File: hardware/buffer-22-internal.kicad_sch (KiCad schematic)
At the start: 9 parts, among them U6 SN74LVC8T245DWRG4, U7 SN74LVC8T245DWRG4, U8 SN74LVC8T245DWRG4

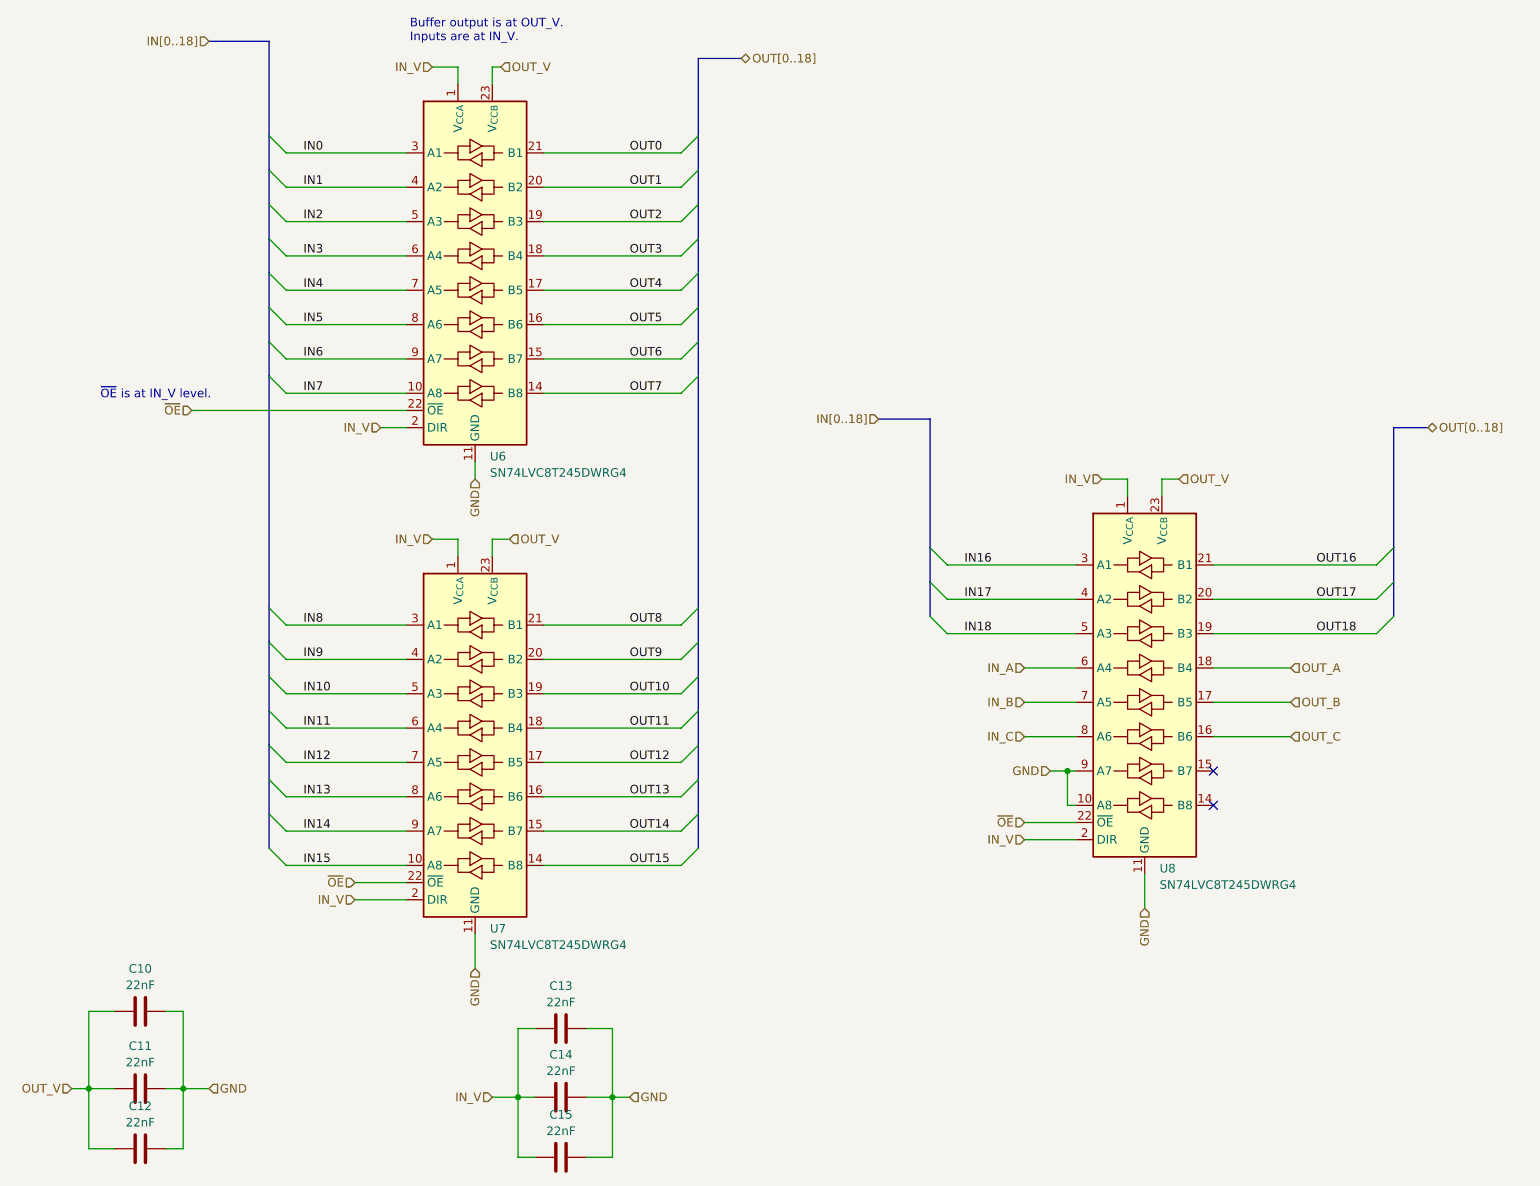
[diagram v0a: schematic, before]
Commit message: Massively reorganize board designs
Now planning to have most assembly done by JLCPCB, so trace sizes,
part selections, etc. are set accordingly.

New boards are:
 - cartridge interface & flash
 - microcontroller & registers
 - sram x2
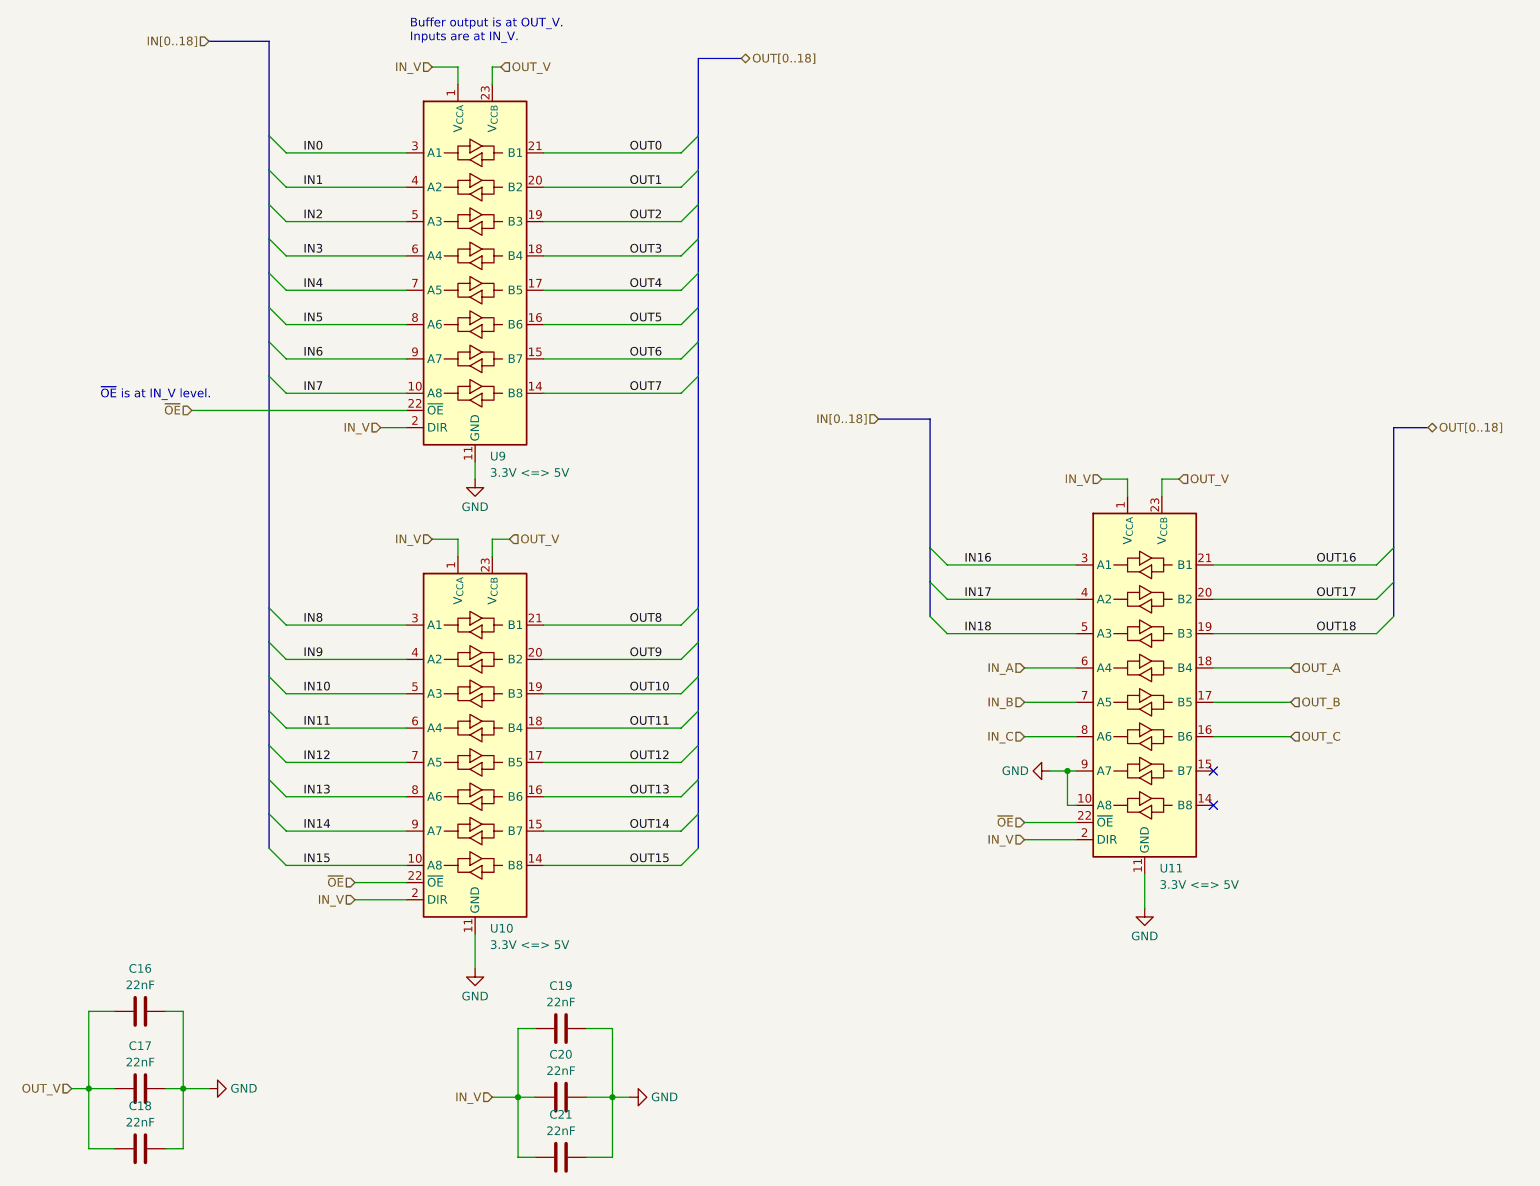
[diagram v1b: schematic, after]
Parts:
- C16: renamed from C10; footprint Capacitor_SMD:C_1206_3216Metric -> Capacitor_SMD:C_0603_1608Metric; JLCPCB Part Number (none) -> CL10B223KB8NNNC; Mouser Part Number (none) -> 80-C0603C223K4R; Part Number (none) -> C0603C223K4RACTU
- C17: renamed from C11; footprint Capacitor_SMD:C_1206_3216Metric -> Capacitor_SMD:C_0603_1608Metric; JLCPCB Part Number (none) -> CL10B223KB8NNNC; Mouser Part Number (none) -> 80-C0603C223K4R; Part Number (none) -> C0603C223K4RACTU
- C18: renamed from C12; footprint Capacitor_SMD:C_1206_3216Metric -> Capacitor_SMD:C_0603_1608Metric; JLCPCB Part Number (none) -> CL10B223KB8NNNC; Mouser Part Number (none) -> 80-C0603C223K4R; Part Number (none) -> C0603C223K4RACTU
- C19: renamed from C13; footprint Capacitor_SMD:C_1206_3216Metric -> Capacitor_SMD:C_0603_1608Metric; JLCPCB Part Number (none) -> CL10B223KB8NNNC; Mouser Part Number (none) -> 80-C0603C223K4R; Part Number (none) -> C0603C223K4RACTU
- C20: renamed from C14; footprint Capacitor_SMD:C_1206_3216Metric -> Capacitor_SMD:C_0603_1608Metric; JLCPCB Part Number (none) -> CL10B223KB8NNNC; Mouser Part Number (none) -> 80-C0603C223K4R; Part Number (none) -> C0603C223K4RACTU
- C21: renamed from C15; footprint Capacitor_SMD:C_1206_3216Metric -> Capacitor_SMD:C_0603_1608Metric; JLCPCB Part Number (none) -> CL10B223KB8NNNC; Mouser Part Number (none) -> 80-C0603C223K4R; Part Number (none) -> C0603C223K4RACTU
- U10: renamed from U7; value SN74LVC8T245DWRG4 -> 3.3V <=> 5V; footprint Package_SO:SOIC-24W_7.5x15.4mm_P1.27mm -> Package_SO:SSOP-24_5.3x8.2mm_P0.65mm; JLCPCB Part Number (none) -> C19197; Mouser Part Number (none) -> 595-SN74LVC8T245DBR; Part Number (none) -> SN74LVC8T245DBR
- U11: renamed from U8; value SN74LVC8T245DWRG4 -> 3.3V <=> 5V; footprint Package_SO:SOIC-24W_7.5x15.4mm_P1.27mm -> Package_SO:SSOP-24_5.3x8.2mm_P0.65mm; JLCPCB Part Number (none) -> C19197; Mouser Part Number (none) -> 595-SN74LVC8T245DBR; Part Number (none) -> SN74LVC8T245DBR
- U9: renamed from U6; value SN74LVC8T245DWRG4 -> 3.3V <=> 5V; footprint Package_SO:SOIC-24W_7.5x15.4mm_P1.27mm -> Package_SO:SSOP-24_5.3x8.2mm_P0.65mm; JLCPCB Part Number (none) -> C19197; Mouser Part Number (none) -> 595-SN74LVC8T245DBR; Part Number (none) -> SN74LVC8T245DBR

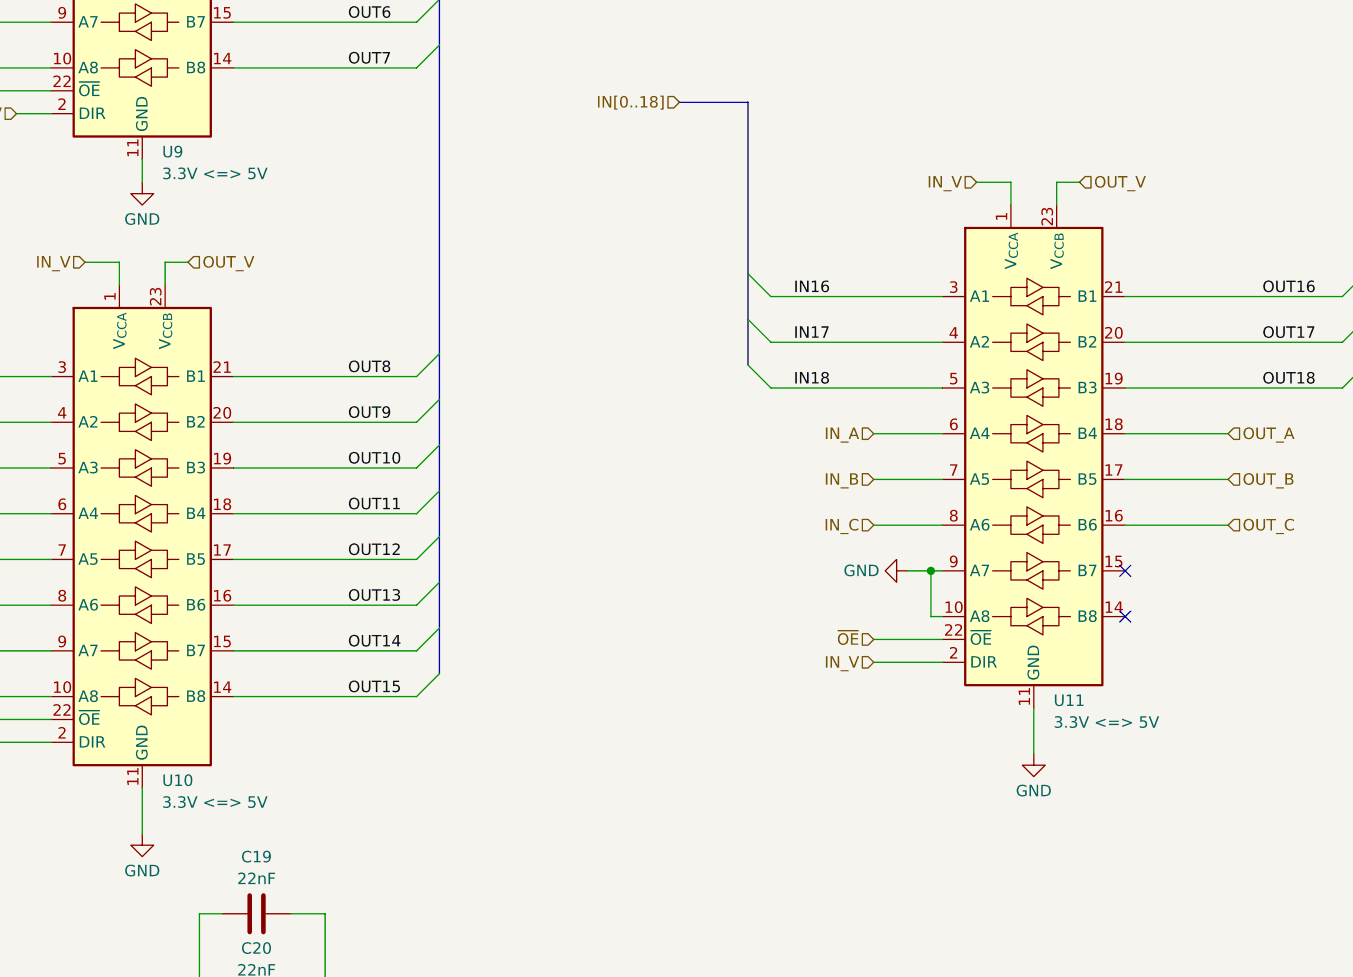
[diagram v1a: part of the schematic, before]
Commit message: Redesign SRAM address decoders
 - Redo original address decoder for SRAM_CE signal
 - Replace NAND gate with another address decoder
   - Simplifies the BOM by removing a one-off part
   - Stabilizes the control signals by making sure SEGA_CONTROL and
     UC_CONTROL can never be active at once (one does not depend on
     the other)
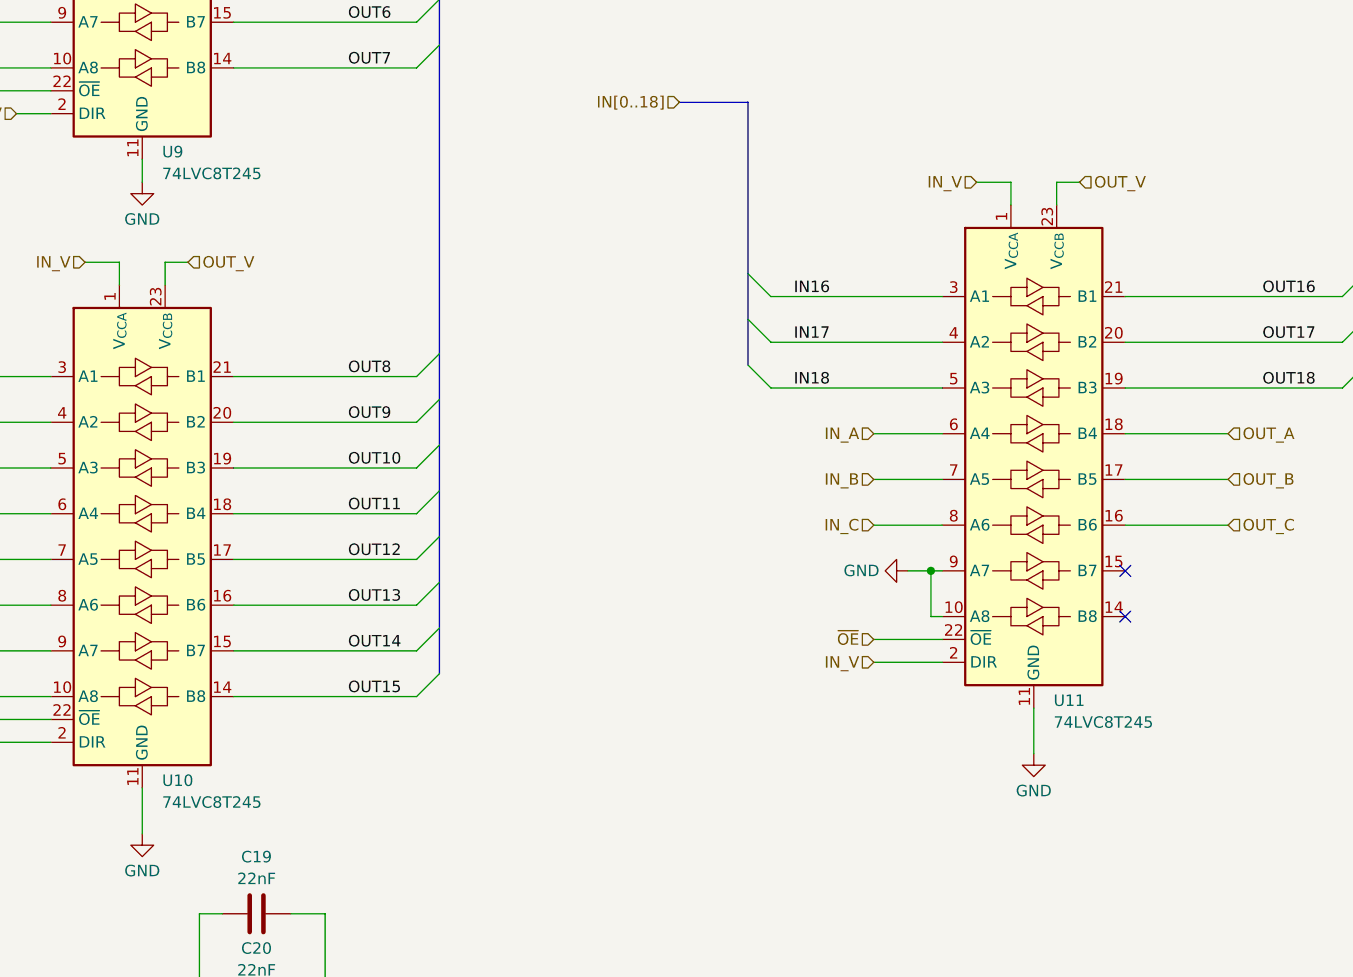
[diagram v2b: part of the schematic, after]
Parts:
- U10, U11, U9: value 3.3V <=> 5V -> 74LVC8T245
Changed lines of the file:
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@@
 			)
 		)
-		(property "Value" "3.3V <=> 5V"
+		(property "Value" "74LVC8T245"
 			(at 190.1541 150.1944 0)
 			(effects
@@
 			)
 		)
-		(property "Value" "3.3V <=> 5V"
+		(property "Value" "74LVC8T245"
 			(at 91.0941 89.2344 0)
 			(effects
@@
 			)
 		)
-		(property "Value" "3.3V <=> 5V"
+		(property "Value" "74LVC8T245"
 			(at 91.0941 159.0844 0)
 			(effects

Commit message: Replace 8-bit buffers with cheaper version
Replace SN74LVC8T245DBR (8-bit buffers) with SN74LVC8T245PWR.  The old
version was SSOP, and the new version is a TSSOP size, but they are
otherwise the same.

This is estimated to reduce the price of a complete unit by over $11,
or about 16.5%.
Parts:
- U10, U11, U9: footprint Package_SO:SSOP-24_5.3x8.2mm_P0.65mm -> Package_SO:TSSOP-24_4.4x7.8mm_P0.65mm; JLCPCB Part Number C19197 -> C27643; Mouser Part Number 595-SN74LVC8T245DBR -> 595-SN74LVC8T245PWR; Part Number SN74LVC8T245DBR -> SN74LVC8T245PWR
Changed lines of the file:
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@@
 			)
 		)
-		(property "Footprint" "Package_SO:SSOP-24_5.3x8.2mm_P0.65mm"
+		(property "Footprint" "Package_SO:TSSOP-24_4.4x7.8mm_P0.65mm"
 			(at 208.28 144.78 0)
 			(effects
@@
 			)
 		)
-		(property "Datasheet" "https://www.ti.com/lit/ds/symlink/sn74lvc8t245.pdf"
+		(property "Datasheet" "https://www.ti.com/lit/gpn/sn74lvc8t245"
 			(at 187.96 156.21 0)
 			(effects
@@
 			)
 		)
-		(property "JLCPCB Part Number" "C19197"
+		(property "JLCPCB Part Number" "C27643"
 			(at 187.96 120.65 0)
 			(effects
@@
 			)
 		)
-		(property "Mouser Part Number" "595-SN74LVC8T245DBR"
+		(property "Mouser Part Number" "595-SN74LVC8T245PWR"
 			(at 187.96 120.65 0)
 			(effects
@@
 			)
 		)
-		(property "Part Number" "SN74LVC8T245DBR"
+		(property "Part Number" "SN74LVC8T245PWR"
 			(at 187.96 120.65 0)
 			(effects
@@
 			)
 		)
-		(property "Footprint" "Package_SO:SSOP-24_5.3x8.2mm_P0.65mm"
+		(property "Footprint" "Package_SO:TSSOP-24_4.4x7.8mm_P0.65mm"
 			(at 109.22 83.82 0)
 			(effects
@@
 			)
 		)
-		(property "Datasheet" "https://www.ti.com/lit/ds/symlink/sn74lvc8t245.pdf"
+		(property "Datasheet" "https://www.ti.com/lit/gpn/sn74lvc8t245"
 			(at 88.9 95.25 0)
 			(effects
@@
 			)
 		)
-		(property "JLCPCB Part Number" "C19197"
+		(property "JLCPCB Part Number" "C27643"
 			(at 88.9 59.69 0)
 			(effects
@@
 			)
 		)
-		(property "Mouser Part Number" "595-SN74LVC8T245DBR"
+		(property "Mouser Part Number" "595-SN74LVC8T245PWR"
 			(at 88.9 59.69 0)
 			(effects
@@
 			)
 		)
-		(property "Part Number" "SN74LVC8T245DBR"
+		(property "Part Number" "SN74LVC8T245PWR"
 			(at 88.9 59.69 0)
 			(effects
@@
 			)
 		)
-		(property "Footprint" "Package_SO:SSOP-24_5.3x8.2mm_P0.65mm"
+		(property "Footprint" "Package_SO:TSSOP-24_4.4x7.8mm_P0.65mm"
 			(at 109.22 153.67 0)
 			(effects
@@
 			)
 		)
-		(property "Datasheet" "https://www.ti.com/lit/ds/symlink/sn74lvc8t245.pdf"
+		(property "Datasheet" "https://www.ti.com/lit/gpn/sn74lvc8t245"
 			(at 88.9 165.1 0)
 			(effects
@@
 			)
 		)
-		(property "JLCPCB Part Number" "C19197"
+		(property "JLCPCB Part Number" "C27643"
 			(at 88.9 129.54 0)
 			(effects
@@
 			)
 		)
-		(property "Mouser Part Number" "595-SN74LVC8T245DBR"
+		(property "Mouser Part Number" "595-SN74LVC8T245PWR"
 			(at 88.9 129.54 0)
 			(effects
@@
 			)
 		)
-		(property "Part Number" "SN74LVC8T245DBR"
+		(property "Part Number" "SN74LVC8T245PWR"
 			(at 88.9 129.54 0)
 			(effects
